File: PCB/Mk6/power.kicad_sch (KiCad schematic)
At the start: 20 parts, among them J1 Power, SW1 RESET, U1 L7805, U2 DS1813, Y25 1.8432 MHz

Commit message: save
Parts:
- renumbered C25 to C10, C26 to C11, C28 to C12, C1 to C13, C2 to C14, C3 to C15, C11 to C2, C12 to C3, C13 to C4, C14 to C5, C15 to C6, C16 to C7, C17 to C8, C18 to C9, J1 to J2, R26 to R2, SW1 to SW2, U1 to U2, U2 to U3, Y25 to Y2
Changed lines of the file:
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@@
 		(dnp no)
 		(fields_autoplaced yes)
-		(property "Reference" "#PWR015"
+		(property "Reference" "#PWR04"
 			(at 140.97 52.07 0)
 			(effects
@@
 			(project "Mk6"
 				(path "/d41350ce-2040-418d-ae11-f076a5474776/c466e200-7308-4cbf-9cc6-0d7b021a89f4"
-					(reference "#PWR015")
+					(reference "#PWR04")
 					(unit 1)
 				)
@@
 		(dnp no)
 		(fields_autoplaced yes)
-		(property "Reference" "#FLG025"
+		(property "Reference" "#FLG02"
 			(at 34.29 28.575 0)
 			(effects
@@
 			(project "Mk6"
 				(path "/d41350ce-2040-418d-ae11-f076a5474776/c466e200-7308-4cbf-9cc6-0d7b021a89f4"
-					(reference "#FLG025")
+					(reference "#FLG02")
 					(unit 1)
 				)
@@
 		(on_board yes)
 		(dnp no)
-		(property "Reference" "C14"
+		(property "Reference" "C5"
 			(at 101.6 34.29 0)
 			(effects
@@
 			(project "Mk6"
 				(path "/d41350ce-2040-418d-ae11-f076a5474776/c466e200-7308-4cbf-9cc6-0d7b021a89f4"
-					(reference "C14")
+					(reference "C5")
 					(unit 1)
 				)
@@
 		(on_board yes)
 		(dnp no)
-		(property "Reference" "J1"
+		(property "Reference" "J2"
 			(at 26.416 29.21 90)
 			(effects
@@
 			(project "Mk6"
 				(path "/d41350ce-2040-418d-ae11-f076a5474776/c466e200-7308-4cbf-9cc6-0d7b021a89f4"
-					(reference "J1")
+					(reference "J2")
 					(unit 1)
 				)
@@
 		(on_board yes)
 		(dnp no)
-		(property "Reference" "C16"
+		(property "Reference" "C7"
 			(at 119.38 34.29 0)
 			(effects
@@
 			(project "Mk6"
 				(path "/d41350ce-2040-418d-ae11-f076a5474776/c466e200-7308-4cbf-9cc6-0d7b021a89f4"
-					(reference "C16")
+					(reference "C7")
 					(unit 1)
 				)
@@
 		(on_board yes)
 		(dnp no)
-		(property "Reference" "C1"
+		(property "Reference" "C13"
 			(at 41.91 37.5538 0)
 			(effects
@@
 			(project "Mk6"
 				(path "/d41350ce-2040-418d-ae11-f076a5474776/c466e200-7308-4cbf-9cc6-0d7b021a89f4"
-					(reference "C1")
+					(reference "C13")
 					(unit 1)
 				)
@@
 		(on_board yes)
 		(dnp no)
-		(property "Reference" "#PWR010"
+		(property "Reference" "#PWR08"
 			(at 81.28 95.25 0)
 			(effects
@@
 			(project "Mk6"
 				(path "/d41350ce-2040-418d-ae11-f076a5474776/c466e200-7308-4cbf-9cc6-0d7b021a89f4"
-					(reference "#PWR010")
+					(reference "#PWR08")
 					(unit 1)
 				)
@@
 		(dnp no)
 		(fields_autoplaced yes)
-		(property "Reference" "#PWR06"
+		(property "Reference" "#PWR05"
 			(at 34.29 53.34 0)
 			(effects
@@
 			(project "Mk6"
 				(path "/d41350ce-2040-418d-ae11-f076a5474776/c466e200-7308-4cbf-9cc6-0d7b021a89f4"
-					(reference "#PWR06")
+					(reference "#PWR05")
 					(unit 1)
 				)
@@
 		(on_board yes)
 		(dnp no)
-		(property "Reference" "C17"
+		(property "Reference" "C8"
 			(at 128.27 34.29 0)
 			(effects
@@
 			(project "Mk6"
 				(path "/d41350ce-2040-418d-ae11-f076a5474776/c466e200-7308-4cbf-9cc6-0d7b021a89f4"
-					(reference "C17")
+					(reference "C8")
 					(unit 1)
 				)
@@
 		(on_board yes)
 		(dnp no)
-		(property "Reference" "C3"
+		(property "Reference" "C15"
 			(at 65.532 36.83 0)
 			(effects
@@
 			(project "Mk6"
 				(path "/d41350ce-2040-418d-ae11-f076a5474776/c466e200-7308-4cbf-9cc6-0d7b021a89f4"
-					(reference "C3")
+					(reference "C15")
 					(unit 1)
 				)
@@
 		(on_board yes)
 		(dnp no)
-		(property "Reference" "C15"
+		(property "Reference" "C6"
 			(at 110.49 34.29 0)
 			(effects
@@
 			(project "Mk6"
 				(path "/d41350ce-2040-418d-ae11-f076a5474776/c466e200-7308-4cbf-9cc6-0d7b021a89f4"
-					(reference "C15")
+					(reference "C6")
 					(unit 1)
 				)
@@
 		(on_board yes)
 		(dnp no)
-		(property "Reference" "C18"
+		(property "Reference" "C9"
 			(at 137.16 34.29 0)
 			(effects
@@
 			(project "Mk6"
 				(path "/d41350ce-2040-418d-ae11-f076a5474776/c466e200-7308-4cbf-9cc6-0d7b021a89f4"
-					(reference "C18")
+					(reference "C9")
 					(unit 1)
 				)
@@
 		(on_board yes)
 		(dnp no)
-		(property "Reference" "C13"
+		(property "Reference" "C4"
 			(at 92.71 34.29 0)
 			(effects
@@
 			(project "Mk6"
 				(path "/d41350ce-2040-418d-ae11-f076a5474776/c466e200-7308-4cbf-9cc6-0d7b021a89f4"
-					(reference "C13")
+					(reference "C4")
 					(unit 1)
 				)
@@
 		(on_board yes)
 		(dnp no)
-		(property "Reference" "C25"
+		(property "Reference" "C10"
 			(at 146.05 34.29 0)
 			(effects
@@
 			(project "Mk6"
 				(path "/d41350ce-2040-418d-ae11-f076a5474776/c466e200-7308-4cbf-9cc6-0d7b021a89f4"
-					(reference "C25")
+					(reference "C10")
 					(unit 1)
 				)
@@
 		(on_board yes)
 		(dnp no)
-		(property "Reference" "C12"
+		(property "Reference" "C3"
 			(at 83.82 34.29 0)
 			(effects
@@
 			(project "Mk6"
 				(path "/d41350ce-2040-418d-ae11-f076a5474776/c466e200-7308-4cbf-9cc6-0d7b021a89f4"
-					(reference "C12")
+					(reference "C3")
 					(unit 1)
 				)
@@
 		(on_board yes)
 		(dnp no)
-		(property "Reference" "#FLG026"
+		(property "Reference" "#FLG03"
 			(at 32.385 36.83 0)
 			(effects
@@
 			(project "Mk6"
 				(path "/d41350ce-2040-418d-ae11-f076a5474776/c466e200-7308-4cbf-9cc6-0d7b021a89f4"
-					(reference "#FLG026")
+					(reference "#FLG03")
 					(unit 1)
 				)
@@
 		(on_board yes)
 		(dnp no)
-		(property "Reference" "C2"
+		(property "Reference" "C14"
 			(at 58.928 37.592 0)
 			(effects
@@
 			(project "Mk6"
 				(path "/d41350ce-2040-418d-ae11-f076a5474776/c466e200-7308-4cbf-9cc6-0d7b021a89f4"
-					(reference "C2")
+					(reference "C14")
 					(unit 1)
 				)
@@
 		(on_board yes)
 		(dnp no)
-		(property "Reference" "C11"
+		(property "Reference" "C2"
 			(at 75.184 34.29 0)
 			(effects
@@
 			(project "Mk6"
 				(path "/d41350ce-2040-418d-ae11-f076a5474776/c466e200-7308-4cbf-9cc6-0d7b021a89f4"
-					(reference "C11")
+					(reference "C2")
 					(unit 1)
 				)
@@
 		(on_board yes)
 		(dnp no)
-		(property "Reference" "#PWR035"
+		(property "Reference" "#PWR06"
 			(at 41.91 66.04 0)
 			(effects
@@
 			(project "Mk6"
 				(path "/d41350ce-2040-418d-ae11-f076a5474776/c466e200-7308-4cbf-9cc6-0d7b021a89f4"
-					(reference "#PWR035")
+					(reference "#PWR06")
 					(unit 1)
 				)
@@
 		(on_board yes)
 		(dnp no)
-		(property "Reference" "SW1"
+		(property "Reference" "SW2"
 			(at 44.45 87.63 0)
 			(effects
@@
 			(project "Mk6"
 				(path "/d41350ce-2040-418d-ae11-f076a5474776/c466e200-7308-4cbf-9cc6-0d7b021a89f4"
-					(reference "SW1")
+					(reference "SW2")
 					(unit 1)
 				)
@@
 		(on_board yes)
 		(dnp no)
-		(property "Reference" "#PWR012"
+		(property "Reference" "#PWR02"
 			(at 78.74 31.75 0)
 			(effects
@@
 			(project "Mk6"
 				(path "/d41350ce-2040-418d-ae11-f076a5474776/c466e200-7308-4cbf-9cc6-0d7b021a89f4"
-					(reference "#PWR012")
+					(reference "#PWR02")
 					(unit 1)
 				)
@@
 		(on_board yes)
 		(dnp no)
-		(property "Reference" "C28"
+		(property "Reference" "C12"
 			(at 175.26 34.29 0)
 			(effects
@@
 			(project "Mk6"
 				(path "/d41350ce-2040-418d-ae11-f076a5474776/c466e200-7308-4cbf-9cc6-0d7b021a89f4"
-					(reference "C28")
+					(reference "C12")
 					(unit 1)
 				)
@@
 		(on_board yes)
 		(dnp no)
-		(property "Reference" "Y25"
+		(property "Reference" "Y2"
 			(at 84.328 67.056 0)
 			(effects
@@
 			(project "Mk6"
 				(path "/d41350ce-2040-418d-ae11-f076a5474776/c466e200-7308-4cbf-9cc6-0d7b021a89f4"
-					(reference "Y25")
+					(reference "Y2")
 					(unit 1)
 				)
@@
 		(on_board yes)
 		(dnp no)
-		(property "Reference" "R26"
+		(property "Reference" "R2"
 			(at 47.498 66.802 90)
 			(effects
@@
 			(project "Mk6"
 				(path "/d41350ce-2040-418d-ae11-f076a5474776/c466e200-7308-4cbf-9cc6-0d7b021a89f4"
-					(reference "R26")
+					(reference "R2")
 					(unit 1)
 				)
@@
 		(on_board yes)
 		(dnp no)
-		(property "Reference" "U2"
+		(property "Reference" "U3"
 			(at 40.894 66.04 0)
 			(effects
@@
 			(project "Mk6"
 				(path "/d41350ce-2040-418d-ae11-f076a5474776/c466e200-7308-4cbf-9cc6-0d7b021a89f4"
-					(reference "U2")
+					(reference "U3")
 					(unit 1)
 				)
@@
 		(dnp no)
 		(fields_autoplaced yes)
-		(property "Reference" "U1"
+		(property "Reference" "U2"
 			(at 49.53 24.13 0)
 			(effects
@@
 			(project "Mk6"
 				(path "/d41350ce-2040-418d-ae11-f076a5474776/c466e200-7308-4cbf-9cc6-0d7b021a89f4"
-					(reference "U1")
+					(reference "U2")
 					(unit 1)
 				)
@@
 		(on_board yes)
 		(dnp no)
-		(property "Reference" "C26"
+		(property "Reference" "C11"
 			(at 155.448 34.29 0)
 			(effects
@@
 			(project "Mk6"
 				(path "/d41350ce-2040-418d-ae11-f076a5474776/c466e200-7308-4cbf-9cc6-0d7b021a89f4"
-					(reference "C26")
+					(reference "C11")
 					(unit 1)
 				)
@@
 		(on_board yes)
 		(dnp no)
-		(property "Reference" "#PWR04"
+		(property "Reference" "#PWR03"
 			(at 62.23 30.48 0)
 			(effects
@@
 			(project "Mk6"
 				(path "/d41350ce-2040-418d-ae11-f076a5474776/c466e200-7308-4cbf-9cc6-0d7b021a89f4"
-					(reference "#PWR04")
-					(unit 1)
-				)
+					(reference "#PWR03")
+					(unit 1)
+				)

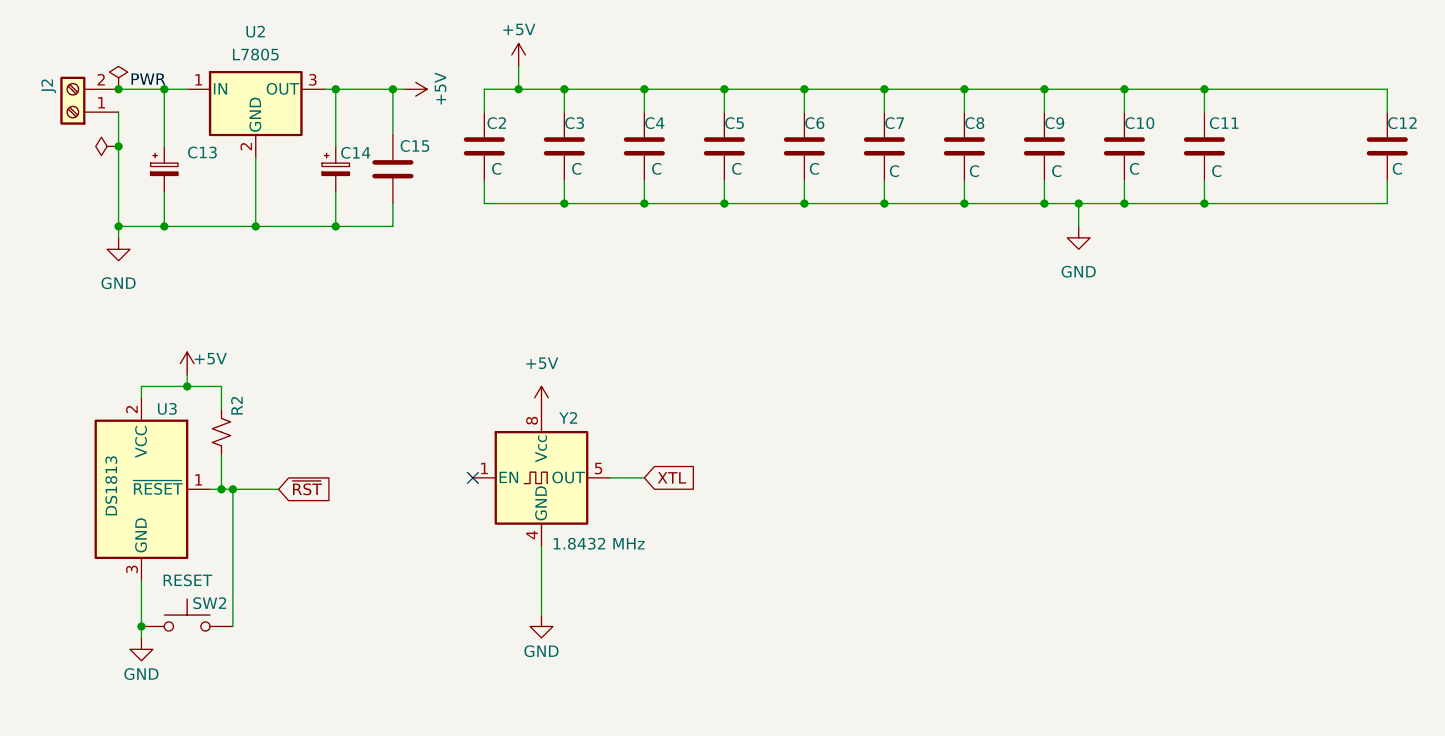
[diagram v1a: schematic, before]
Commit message: all done, pre-clk div
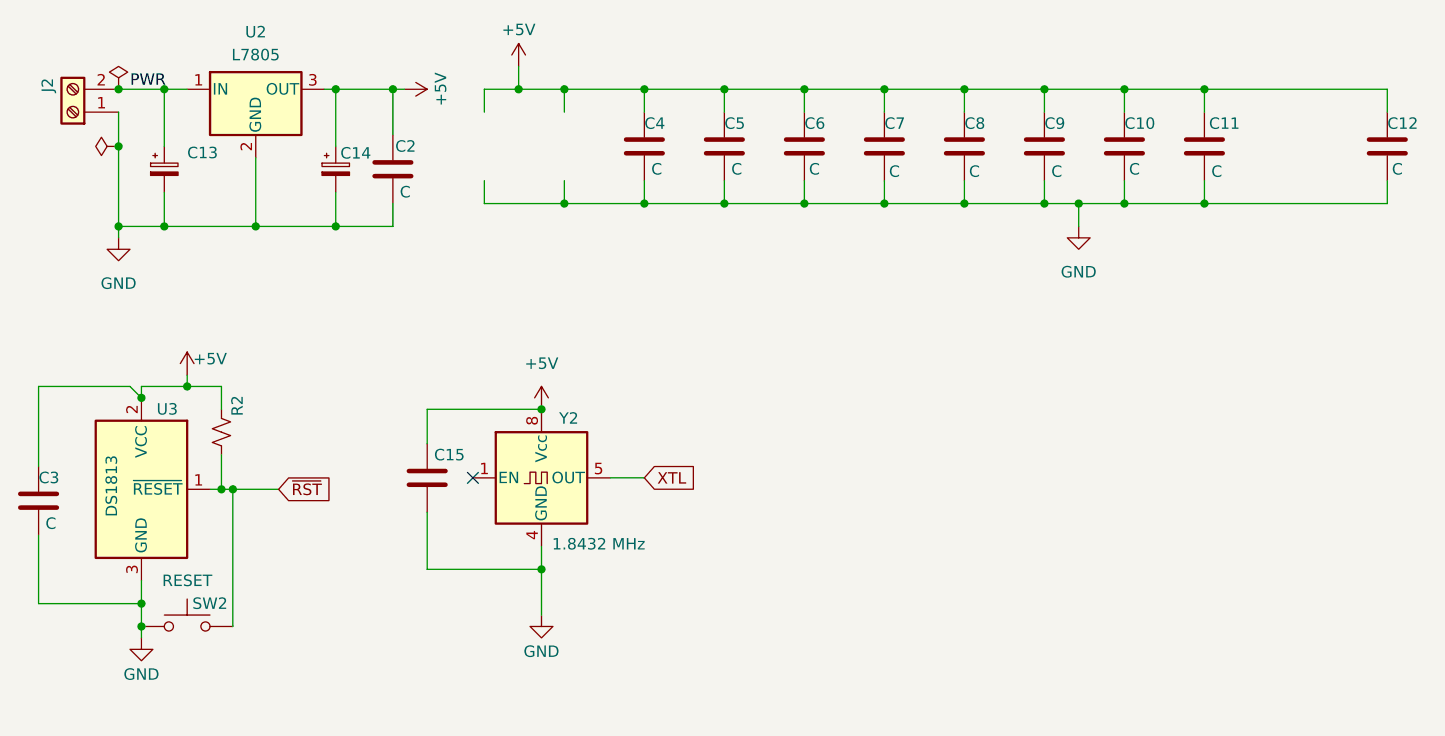
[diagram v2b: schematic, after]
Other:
- moved on the sheet: C15, C2, C3
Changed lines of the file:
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@@
 	(paper "A4")
 	(junction
+		(at 81.28 66.04)
+		(diameter 0)
+		(color 0 0 0 0)
+	)
+	(junction
 		(at 137.16 30.48)
 		(diameter 0)
@@
 	)
 	(junction
+		(at 36.83 87.63)
+		(diameter 0)
+		(color 0 0 0 0)
+	)
+	(junction
 		(at 49.53 45.72)
 		(diameter 0)
@@
 	)
 	(junction
+		(at 81.28 83.82)
+		(diameter 0)
+		(color 0 0 0 0)
+	)
+	(junction
 		(at 119.38 30.48)
 		(diameter 0)
@@
 	(junction
 		(at 83.82 30.48)
+		(diameter 0)
+		(color 0 0 0 0)
+	)
+	(junction
+		(at 36.83 64.77)
 		(diameter 0)
 		(color 0 0 0 0)
@@
 	(wire
 		(pts
-			(xy 81.28 88.9) (xy 81.28 81.28)
+			(xy 81.28 88.9) (xy 81.28 83.82)
 		)
 		(stroke
@@
 	(wire
 		(pts
+			(xy 68.58 77.47) (xy 68.58 83.82)
+		)
+		(stroke
+			(width 0)
+			(type default)
+		)
+	)
+	(wire
+		(pts
 			(xy 146.05 43.18) (xy 146.05 40.64)
 		)
@@
 	(wire
 		(pts
+			(xy 25.4 80.01) (xy 25.4 87.63)
+		)
+		(stroke
+			(width 0)
+			(type default)
+		)
+	)
+	(wire
+		(pts
 			(xy 74.93 30.48) (xy 78.74 30.48)
 		)
@@
 	(wire
 		(pts
+			(xy 25.4 63.5) (xy 25.4 72.39)
+		)
+		(stroke
+			(width 0)
+			(type default)
+		)
+	)
+	(wire
+		(pts
 			(xy 119.38 33.02) (xy 119.38 30.48)
 		)
@@
 	(wire
 		(pts
-			(xy 36.83 85.09) (xy 36.83 90.17)
+			(xy 36.83 85.09) (xy 36.83 87.63)
 		)
 		(stroke
@@
 	(wire
 		(pts
+			(xy 68.58 66.04) (xy 81.28 66.04)
+		)
+		(stroke
+			(width 0)
+			(type default)
+		)
+	)
+	(wire
+		(pts
 			(xy 78.74 30.48) (xy 83.82 30.48)
 		)
@@
 	(wire
 		(pts
+			(xy 68.58 66.04) (xy 68.58 69.85)
+		)
+		(stroke
+			(width 0)
+			(type default)
+		)
+	)
+	(wire
+		(pts
+			(xy 81.28 83.82) (xy 81.28 81.28)
+		)
+		(stroke
+			(width 0)
+			(type default)
+		)
+	)
+	(wire
+		(pts
 			(xy 36.83 63.5) (xy 41.91 63.5)
 		)
@@
 	(wire
 		(pts
+			(xy 35.56 63.5) (xy 36.83 64.77)
+		)
+		(stroke
+			(width 0)
+			(type default)
+		)
+	)
+	(wire
+		(pts
 			(xy 128.27 33.02) (xy 128.27 30.48)
 		)
@@
 	(wire
 		(pts
+			(xy 36.83 87.63) (xy 36.83 90.17)
+		)
+		(stroke
+			(width 0)
+			(type default)
+		)
+	)
+	(wire
+		(pts
 			(xy 119.38 30.48) (xy 128.27 30.48)
 		)
@@
 	(wire
 		(pts
+			(xy 25.4 87.63) (xy 36.83 87.63)
+		)
+		(stroke
+			(width 0)
+			(type default)
+		)
+	)
+	(wire
+		(pts
 			(xy 146.05 43.18) (xy 154.94 43.18)
 		)
@@
 	(wire
 		(pts
+			(xy 68.58 83.82) (xy 81.28 83.82)
+		)
+		(stroke
+			(width 0)
+			(type default)
+		)
+	)
+	(wire
+		(pts
 			(xy 39.37 45.72) (xy 49.53 45.72)
 		)
@@
 		(pts
 			(xy 58.42 45.72) (xy 58.42 41.91)
+		)
+		(stroke
+			(width 0)
+			(type default)
+		)
+	)
+	(wire
+		(pts
+			(xy 25.4 63.5) (xy 35.56 63.5)
 		)
 		(stroke
@@
 	(symbol
 		(lib_id "Device:C")
-		(at 64.77 39.37 0)
+		(at 68.58 73.66 0)
 		(unit 1)
 		(exclude_from_sim no)
@@
 		(dnp no)
 		(property "Reference" "C15"
-			(at 65.532 36.83 0)
+			(at 69.342 71.12 0)
 			(effects
 				(font
@@
 		)
 		(property "Value" "C"
-			(at 65.532 41.656 0)
+			(at 69.342 75.946 0)
 			(effects
 				(font
@@
 		)
 		(property "Footprint" "Capacitor_THT:C_Disc_D7.5mm_W2.5mm_P5.00mm"
-			(at 65.7352 43.18 0)
+			(at 69.5452 77.47 0)
 			(effects
 				(font
@@
 		)
 		(property "Datasheet" "~"
-			(at 64.77 39.37 0)
+			(at 68.58 73.66 0)
 			(effects
 				(font
@@
 		)
 		(property "Description" "Unpolarized capacitor"
-			(at 64.77 39.37 0)
+			(at 68.58 73.66 0)
 			(effects
 				(font
@@
 	(symbol
 		(lib_id "Device:C")
-		(at 83.82 36.83 0)
+		(at 25.4 76.2 0)
 		(unit 1)
 		(exclude_from_sim no)
@@
 		(dnp no)
 		(property "Reference" "C3"
-			(at 83.82 34.29 0)
+			(at 25.4 73.66 0)
 			(effects
 				(font
@@
 		)
 		(property "Value" "C"
-			(at 84.582 39.37 0)
+			(at 26.162 78.74 0)
 			(effects
 				(font
@@
 		)
 		(property "Footprint" "Capacitor_THT:C_Disc_D7.5mm_W2.5mm_P5.00mm"
-			(at 84.7852 40.64 0)
+			(at 26.3652 80.01 0)
 			(effects
 				(font
@@
 		)
 		(property "Datasheet" "~"
-			(at 83.82 36.83 0)
+			(at 25.4 76.2 0)
 			(effects
 				(font
@@
 		)
 		(property "Description" "Unpolarized capacitor"
-			(at 83.82 36.83 0)
+			(at 25.4 76.2 0)
 			(effects
 				(font
@@
 	(symbol
 		(lib_id "Device:C")
-		(at 74.93 36.83 0)
+		(at 64.77 39.37 0)
 		(unit 1)
 		(exclude_from_sim no)
@@
 		(dnp no)
 		(property "Reference" "C2"
-			(at 75.184 34.29 0)
+			(at 65.024 36.83 0)
 			(effects
 				(font
@@
 		)
 		(property "Value" "C"
-			(at 75.692 39.37 0)
+			(at 65.532 41.91 0)
 			(effects
 				(font
@@
 		)
 		(property "Footprint" "Capacitor_THT:C_Disc_D7.5mm_W2.5mm_P5.00mm"
-			(at 75.8952 40.64 0)
+			(at 65.7352 43.18 0)
 			(effects
 				(font
@@
 		)
 		(property "Datasheet" "~"
-			(at 74.93 36.83 0)
+			(at 64.77 39.37 0)
 			(effects
 				(font
@@
 		)
 		(property "Description" "Unpolarized capacitor"
-			(at 74.93 36.83 0)
-			(effects
-				(font
+			(at 64.77 39.37 0)
+			(effects
+				(font

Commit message: Cleaned
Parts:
- added JP1843: 1843, Connector_PinHeader_2.54mm:PinHeader_1x02_P2.54mm_Vertical, symbol RetroParts_Library:Jumper_2_Open
- added JP450: 450, Connector_PinHeader_2.54mm:PinHeader_1x02_P2.54mm_Vertical, symbol RetroParts_Library:Jumper_2_Open
- added JP921: 921, Connector_PinHeader_2.54mm:PinHeader_1x02_P2.54mm_Vertical, symbol RetroParts_Library:Jumper_2_Open
- added U7: 74LS92, Package_DIP:DIP-14_W7.62mm_LongPads, symbol 74xx:74LS92
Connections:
- net +5V: now also U7.5 (VCC)
- net GND: now also U7.10 (GND), U7.6 (R0(1)), U7.7 (R0(2))
- net XTL: no longer names the net of Y2.5 (OUT)
- net XTL: now also JP1843.1 (A), U7.14 (CP0)
- new net: JP921.1 (A), U7.1 (CP1..3), U7.12 (Q0)
- new net: JP450.1 (A), U7.9 (Q2)
- new net BaudClk: U7.8 (Q3)
- new net Clk0: JP1843.2 (B), JP450.2 (B), JP921.2 (B)
- no-connect marks 1 -> 2
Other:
- note added: "153600Hz 9600/2400"

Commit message: Added LCD cap
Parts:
- added C16: C, Capacitor_THT:C_Disc_D7.5mm_W2.5mm_P5.00mm, symbol Device:C
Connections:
- net +5V: now also C16.1
- net GND: now also C16.2
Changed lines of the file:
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@@
+	)
+	(junction
+		(at 163.83 30.48)
+		(diameter 0)
+		(color 0 0 0 0)
 	)
 	(junction
@@
 	(junction
 		(at 64.77 30.48)
+		(diameter 0)
+		(color 0 0 0 0)
+	)
+	(junction
+		(at 163.83 43.18)
 		(diameter 0)
 		(color 0 0 0 0)
@@
 	(wire
 		(pts
+			(xy 163.83 40.64) (xy 163.83 43.18)
+		)
+		(stroke
+			(width 0)
+			(type default)
+		)
+	)
+	(wire
+		(pts
 			(xy 36.83 85.09) (xy 36.83 87.63)
 		)
@@
 	(wire
 		(pts
+			(xy 163.83 30.48) (xy 163.83 33.02)
+		)
+		(stroke
+			(width 0)
+			(type default)
+		)
+	)
+	(wire
+		(pts
 			(xy 128.27 33.02) (xy 128.27 30.48)
 		)
@@
 	(wire
 		(pts
+			(xy 163.83 30.48) (xy 175.26 30.48)
+		)
+		(stroke
+			(width 0)
+			(type default)
+		)
+	)
+	(wire
+		(pts
 			(xy 91.44 73.66) (xy 88.9 73.66)
 		)
@@
 	(wire
 		(pts
+			(xy 163.83 43.18) (xy 175.26 43.18)
+		)
+		(stroke
+			(width 0)
+			(type default)
+		)
+	)
+	(wire
+		(pts
 			(xy 36.83 87.63) (xy 36.83 90.17)
 		)
@@
 	(wire
 		(pts
-			(xy 154.94 43.18) (xy 175.26 43.18)
+			(xy 154.94 43.18) (xy 163.83 43.18)
 		)
 		(stroke
@@
 	(wire
 		(pts
-			(xy 154.94 30.48) (xy 175.26 30.48)
+			(xy 154.94 30.48) (xy 163.83 30.48)
 		)
 		(stroke
@@
 					(unit 1)
 				)
+			)
+		)
+	)
+	(symbol
+		(lib_id "Device:C")
+		(at 163.83 36.83 0)
+		(unit 1)
+		(exclude_from_sim no)
+		(in_bom yes)
+		(on_board yes)
+		(dnp no)
+		(property "Reference" "C16"
+			(at 164.338 34.29 0)
+			(effects
+				(font
+					(size 1.27 1.27)
+				)
+				(justify left)
+			)
+		)
+		(property "Value" "C"
+			(at 164.592 39.624 0)
+			(effects
+				(font
+					(size 1.27 1.27)
+				)
+				(justify left)
+			)
+		)
+		(property "Footprint" "Capacitor_THT:C_Disc_D7.5mm_W2.5mm_P5.00mm"
+			(at 164.7952 40.64 0)
+			(effects
+				(font
+					(size 1.27 1.27)
+				)
+				(hide yes)
+			)
+		)
+		(property "Datasheet" "~"
+			(at 163.83 36.83 0)
+			(effects
+				(font
+					(size 1.27 1.27)
+				)
+				(hide yes)
+			)
+		)
+		(property "Description" "Unpolarized capacitor"
+			(at 163.83 36.83 0)
+			(effects
+				(font
+					(size 1.27 1.27)
+				)
+				(hide yes)
+			)
+		)
+		(pin "2"
+		)
+		(pin "1"
+		)
+		(instances
+			(project "Mk6"
+				(path "/d41350ce-2040-418d-ae11-f076a5474776/c466e200-7308-4cbf-9cc6-0d7b021a89f4"
+					(reference "C16")
+					(unit 1)
+				)

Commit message: Pre Remap
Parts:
- removed JP1843: 1843, Connector_PinHeader_2.54mm:PinHeader_1x02_P2.54mm_Vertical, symbol RetroParts_Library:Jumper_2_Open
- removed JP450: 450, Connector_PinHeader_2.54mm:PinHeader_1x02_P2.54mm_Vertical, symbol RetroParts_Library:Jumper_2_Open
- removed JP921: 921, Connector_PinHeader_2.54mm:PinHeader_1x02_P2.54mm_Vertical, symbol RetroParts_Library:Jumper_2_Open
- added JP3: 1.8-M-0.9, Connector_PinHeader_2.54mm:PinHeader_1x03_P2.54mm_Vertical, symbol Jumper:Jumper_3_Open
- added JP4: 19200 / 9600, Connector_PinHeader_2.54mm:PinHeader_1x03_P2.54mm_Vertical, symbol Jumper:Jumper_3_Open
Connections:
- net BaudClk: now also JP4.2 (C); no longer U7.8 (Q3)
- net Clk0: now also JP3.2 (C)
- net at U7.1 (CP1..3), U7.12 (Q0): now also JP3.3 (B), JP4.3 (B)
- net at U7.14 (CP0), Y2.5 (OUT): now also JP3.1 (A)
- new net: JP4.1 (A), U7.8 (Q3)
- no-connect marks 2 -> 3
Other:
- note added: "19200/4800"
